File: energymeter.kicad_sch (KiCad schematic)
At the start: 43 parts, among them J1 CT1, J10 CT10, J11 LINE, J12 Conn_02x09_Odd_Even, J13 Conn_02x09_Odd_Even, J2 CT2, J3 CT3, J4 CT4, J5 CT5, J6 CT6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

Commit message: Updates
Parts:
- added J14: NEUTRAL, TerminalBlock_Phoenix:TerminalBlock_Phoenix_MKDS-1,5-2_1x02_P5.00mm_Horizontal, symbol Connector:Screw_Terminal_01x02
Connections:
- net at T1.2: now also J14.1 (Pin_1), J14.2 (Pin_2); no longer R67.1
- net at J11.1 (Pin_1), R65.2: now also J11.2 (Pin_2)
- net at R63.2: now also R67.1; no longer J11.2 (Pin_2)
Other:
- moved on the sheet: R65, R66, R67
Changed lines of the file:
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@@
 	)
 	(junction
-		(at 116.84 158.75)
+		(at 87.63 166.37)
 		(diameter 0)
 		(color 0 0 0 0)
@@
 	)
 	(junction
+		(at 87.63 153.67)
+		(diameter 0)
+		(color 0 0 0 0)
+	)
+	(junction
 		(at 162.56 144.78)
 		(diameter 0)
@@
 	(wire
 		(pts
-			(xy 97.79 158.75) (xy 99.06 158.75)
-		)
-		(stroke
-			(width 0)
-			(type default)
-		)
-	)
-	(wire
-		(pts
-			(xy 87.63 158.75) (xy 90.17 158.75)
+			(xy 97.79 153.67) (xy 99.06 153.67)
 		)
 		(stroke
@@
 	(wire
 		(pts
-			(xy 116.84 158.75) (xy 115.57 158.75)
+			(xy 116.84 166.37) (xy 87.63 166.37)
 		)
 		(stroke
@@
 	(wire
 		(pts
+			(xy 87.63 166.37) (xy 87.63 167.64)
+		)
+		(stroke
+			(width 0)
+			(type default)
+		)
+	)
+	(wire
+		(pts
+			(xy 115.57 153.67) (xy 116.84 153.67)
+		)
+		(stroke
+			(width 0)
+			(type default)
+		)
+	)
+	(wire
+		(pts
 			(xy 127 144.78) (xy 140.97 144.78)
 		)
@@
 	(wire
 		(pts
+			(xy 87.63 165.1) (xy 87.63 166.37)
+		)
+		(stroke
+			(width 0)
+			(type default)
+		)
+	)
+	(wire
+		(pts
 			(xy 105.41 38.1) (xy 105.41 41.91)
 		)
@@
 	(wire
 		(pts
+			(xy 87.63 152.4) (xy 87.63 153.67)
+		)
+		(stroke
+			(width 0)
+			(type default)
+		)
+	)
+	(wire
+		(pts
 			(xy 102.87 88.9) (xy 110.49 88.9)
 		)
@@
 	(wire
 		(pts
+			(xy 95.25 151.13) (xy 116.84 151.13)
+		)
+		(stroke
+			(width 0)
+			(type default)
+		)
+	)
+	(wire
+		(pts
 			(xy 217.17 144.78) (xy 217.17 146.05)
 		)
@@
 	(wire
 		(pts
-			(xy 106.68 158.75) (xy 107.95 158.75)
+			(xy 106.68 153.67) (xy 107.95 153.67)
 		)
 		(stroke
@@
 	(wire
 		(pts
+			(xy 116.84 151.13) (xy 116.84 153.67)
+		)
+		(stroke
+			(width 0)
+			(type default)
+		)
+	)
+	(wire
+		(pts
 			(xy 59.69 118.11) (xy 63.5 118.11)
 		)
@@
 	(wire
 		(pts
+			(xy 116.84 158.75) (xy 116.84 166.37)
+		)
+		(stroke
+			(width 0)
+			(type default)
+		)
+	)
+	(wire
+		(pts
 			(xy 27.94 29.21) (xy 27.94 27.94)
 		)
@@
 	(wire
 		(pts
-			(xy 119.38 158.75) (xy 116.84 158.75)
+			(xy 162.56 144.78) (xy 152.4 144.78)
 		)
 		(stroke
@@
 	(wire
 		(pts
-			(xy 162.56 144.78) (xy 152.4 144.78)
+			(xy 90.17 153.67) (xy 87.63 153.67)
 		)
 		(stroke
@@
 	(wire
 		(pts
+			(xy 87.63 153.67) (xy 87.63 154.94)
+		)
+		(stroke
+			(width 0)
+			(type default)
+		)
+	)
+	(wire
+		(pts
 			(xy 140.97 144.78) (xy 140.97 149.86)
 		)
@@
 	(wire
 		(pts
-			(xy 87.63 158.75) (xy 87.63 154.94)
-		)
-		(stroke
-			(width 0)
-			(type default)
-		)
-	)
-	(wire
-		(pts
 			(xy 218.44 95.25) (xy 218.44 97.79)
 		)
@@
 	(wire
 		(pts
-			(xy 87.63 148.59) (xy 87.63 152.4)
-		)
-		(stroke
-			(width 0)
-			(type default)
-		)
-	)
-	(wire
-		(pts
 			(xy 143.51 104.14) (xy 143.51 110.49)
 		)
@@
 	(wire
 		(pts
-			(xy 95.25 148.59) (xy 87.63 148.59)
-		)
-		(stroke
-			(width 0)
-			(type default)
-		)
-	)
-	(wire
-		(pts
 			(xy 218.44 57.15) (xy 220.98 57.15)
 		)
@@
 	(wire
 		(pts
+			(xy 95.25 148.59) (xy 95.25 151.13)
+		)
+		(stroke
+			(width 0)
+			(type default)
+		)
+	)
+	(wire
+		(pts
 			(xy 218.44 41.91) (xy 220.98 41.91)
 		)
@@
 	)
 	(symbol
+		(lib_id "Connector:Screw_Terminal_01x02")
+		(at 82.55 167.64 180)
+		(unit 1)
+		(exclude_from_sim no)
+		(in_bom yes)
+		(on_board yes)
+		(dnp no)
+		(fields_autoplaced yes)
+		(property "Reference" "J14"
+			(at 82.55 158.75 0)
+			(effects
+				(font
+					(size 1.27 1.27)
+				)
+			)
+		)
+		(property "Value" "NEUTRAL"
+			(at 82.55 161.29 0)
+			(effects
+				(font
+					(size 1.27 1.27)
+				)
+			)
+		)
+		(property "Footprint" "TerminalBlock_Phoenix:TerminalBlock_Phoenix_MKDS-1,5-2_1x02_P5.00mm_Horizontal"
+			(at 82.55 167.64 0)
+			(effects
+				(font
+					(size 1.27 1.27)
+				)
+				(hide yes)
+			)
+		)
+		(property "Datasheet" "~"
+			(at 82.55 167.64 0)
+			(effects
+				(font
+					(size 1.27 1.27)
+				)
+				(hide yes)
+			)
+		)
+		(property "Description" "Generic screw terminal, single row, 01x02, script generated (kicad-library-utils/schlib/autogen/connector/)"
+			(at 82.55 167.64 0)
+			(effects
+				(font
+					(size 1.27 1.27)
+				)
+				(hide yes)
+			)
+		)
+		(pin "2"
+		)
+		(pin "1"
+		)
+		(instances
+			(project "energymeter"
+				(path "/d5c3d4dc-7952-499c-ae9a-397827d02ad2"
+					(reference "J14")
+					(unit 1)
+				)
+			)
+		)
+	)
+	(symbol
 		(lib_id "power:+3.3V")
 		(at 259.08 128.27 0)
@@
 	(symbol
 		(lib_id "Device:R")
-		(at 111.76 158.75 270)
+		(at 111.76 153.67 270)
 		(unit 1)
 		(exclude_from_sim no)
@@
 		(fields_autoplaced yes)
 		(property "Reference" "R67"
-			(at 111.76 165.1 90)
+			(at 111.76 160.02 90)
 			(effects
 				(font
@@
 		)
 		(property "Value" "22K/1%"
-			(at 111.76 162.56 90)
+			(at 111.76 157.48 90)
 			(effects
 				(font
@@
 		)
 		(property "Footprint" "Resistor_SMD:R_0603_1608Metric"
-			(at 111.76 156.972 90)
+			(at 111.76 151.892 90)
 			(effects
 				(font
@@
 		)
 		(property "Datasheet" "~"
-			(at 111.76 158.75 0)
+			(at 111.76 153.67 0)
 			(effects
 				(font
@@
 		)
 		(property "Description" "Resistor"
-			(at 111.76 158.75 0)
+			(at 111.76 153.67 0)
 			(effects
 				(font
@@
 	(symbol
 		(lib_id "Device:R")
-		(at 102.87 158.75 270)
+		(at 102.87 153.67 270)
 		(unit 1)
 		(exclude_from_sim no)
@@
 		(fields_autoplaced yes)
 		(property "Reference" "R66"
-			(at 102.87 165.1 90)
+			(at 102.87 160.02 90)
 			(effects
 				(font
@@
 		)
 		(property "Value" "22K/1%"
-			(at 102.87 162.56 90)
+			(at 102.87 157.48 90)
 			(effects
 				(font
@@
 		)
 		(property "Footprint" "Resistor_SMD:R_0603_1608Metric"
-			(at 102.87 156.972 90)
+			(at 102.87 151.892 90)
 			(effects
 				(font
@@
 		)
 		(property "Datasheet" "~"
-			(at 102.87 158.75 0)
+			(at 102.87 153.67 0)
 			(effects
 				(font
@@
 		)
 		(property "Description" "Resistor"
-			(at 102.87 158.75 0)
+			(at 102.87 153.67 0)
 			(effects
 				(font
@@
 	(symbol
 		(lib_id "Device:R")
-		(at 93.98 158.75 270)
+		(at 93.98 153.67 270)
 		(unit 1)
 		(exclude_from_sim no)
@@
 		(fields_autoplaced yes)
 		(property "Reference" "R65"
-			(at 93.98 165.1 90)
+			(at 93.98 160.02 90)
 			(effects
 				(font
@@
 		)
 		(property "Value" "22K/1%"
-			(at 93.98 162.56 90)
+			(at 93.98 157.48 90)
 			(effects
 				(font
@@
 		)
 		(property "Footprint" "Resistor_SMD:R_0603_1608Metric"
-			(at 93.98 156.972 90)
+			(at 93.98 151.892 90)
 			(effects
 				(font
@@
 		)
 		(property "Datasheet" "~"
-			(at 93.98 158.75 0)
+			(at 93.98 153.67 0)
 			(effects
 				(font
@@
 		)
 		(property "Description" "Resistor"
-			(at 93.98 158.75 0)
+			(at 93.98 153.67 0)
 			(effects
 				(font

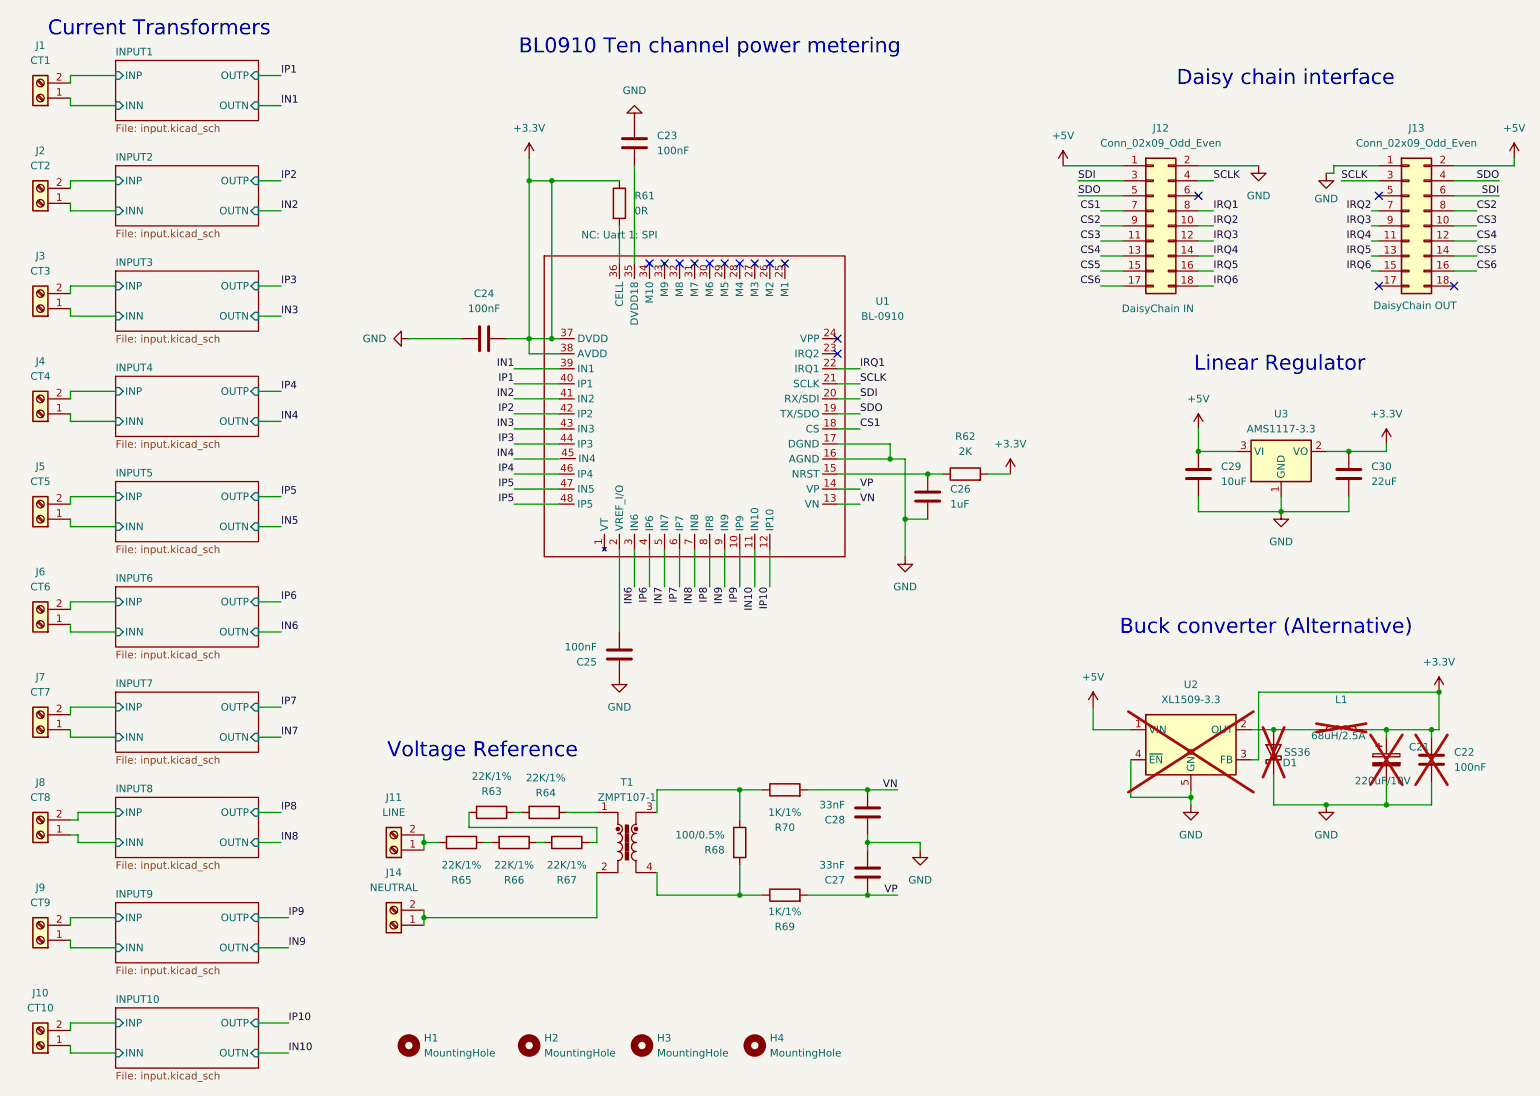
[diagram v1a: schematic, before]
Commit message: Change connector, assign JLCPCB
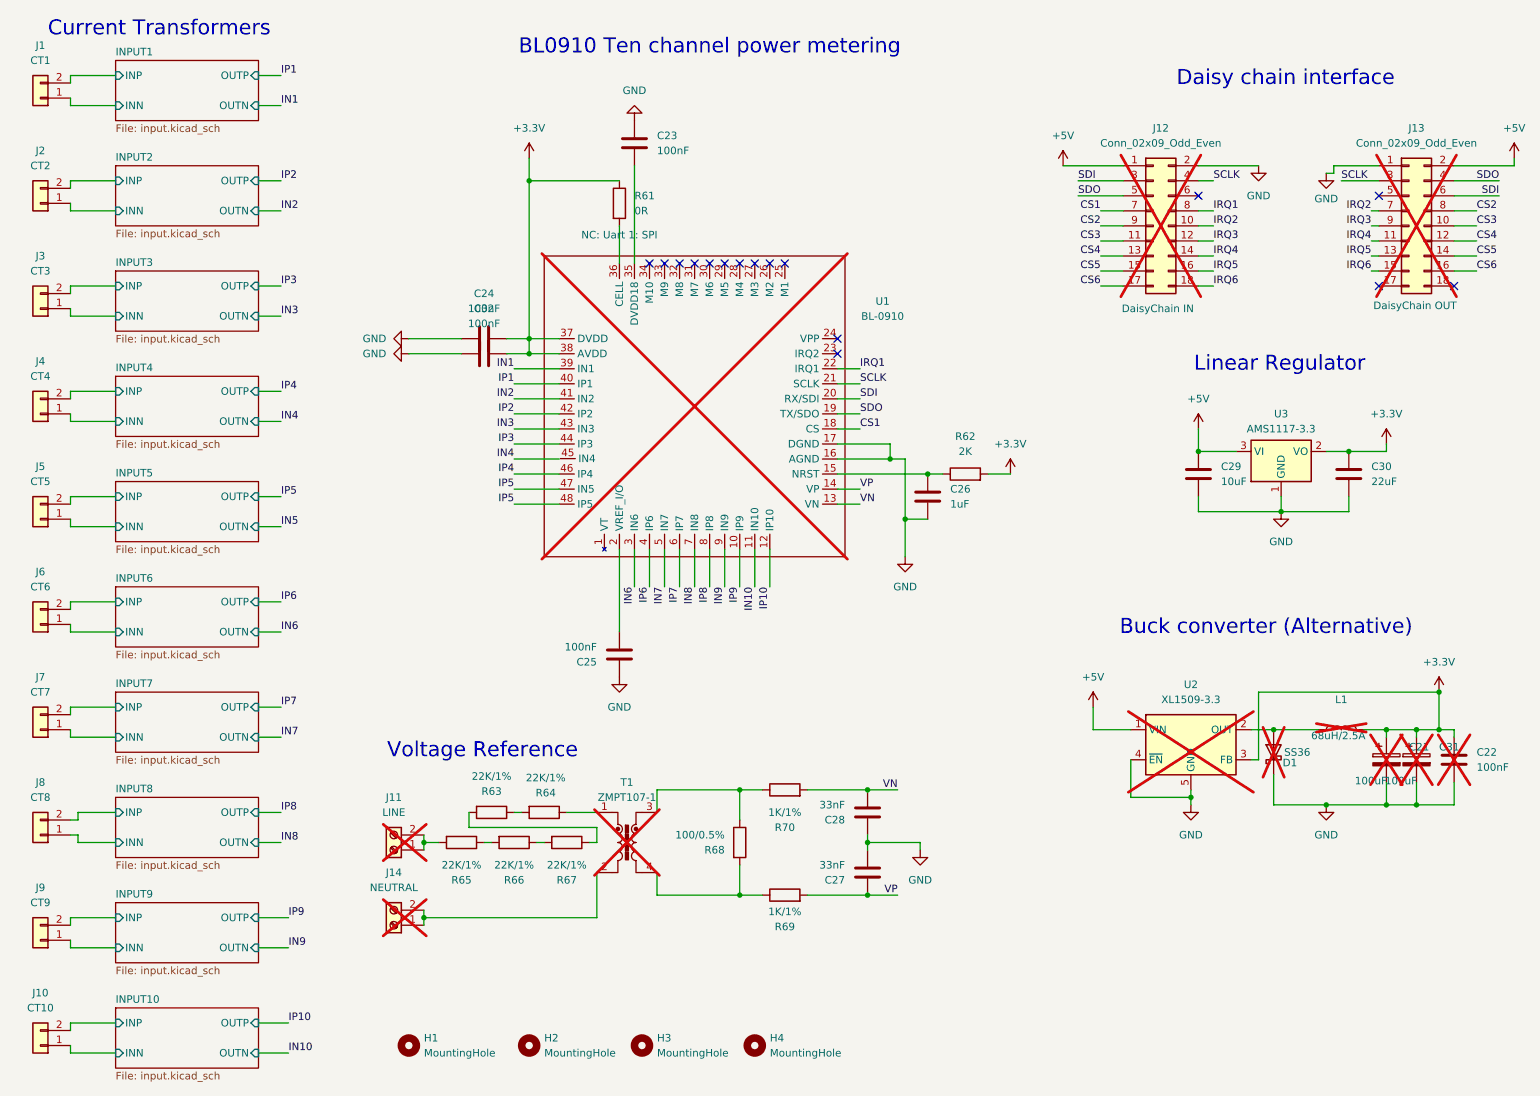
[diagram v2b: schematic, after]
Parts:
- added C31: 100uF, Capacitor_Tantalum_SMD:CP_EIA-3528-21_Kemet-B, symbol Device:C_Polarized
- added C32: 100nF, Capacitor_SMD:C_0603_1608Metric, symbol Device:C
- C21: value 220uF/10V -> 100uF; footprint (none) -> Capacitor_Tantalum_SMD:CP_EIA-3528-21_Kemet-B; LCSC (none) -> C16133
- C22, C23, C24, C25, C29: LCSC (none) -> C14858
- C26: LCSC (none) -> C15849
- C27, C28: LCSC (none) -> C21117
- C30: LCSC (none) -> C59461
- J1, J10, J2, J3, J4, J5, J6, J7, J8, J9: footprint TerminalBlock_Phoenix:TerminalBlock_Phoenix_MKDS-1,5-2_1x02_P5.00mm_Horizontal -> Connector_JST:JST_XH_B2B-XH-A_1x02_P2.50mm_Vertical; symbol Connector:Screw_Terminal_01x02 -> Connector_Generic:Conn_01x02; LCSC (none) -> C265283
- J11, J12, J13, J14, U1: now not fitted
- R61: LCSC (none) -> C21189
- R62: LCSC (none) -> C22975
- R63, R64, R65, R66, R67: LCSC (none) -> C31850
- R68: LCSC (none) -> C22775
- R69, R70: LCSC (none) -> C21190
- T1: LCSC (none) -> C125191; now not fitted
- U2: JLCPCB C61063 -> (none); LCSC (none) -> C61063
- U3: LCSC (none) -> C6186
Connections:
- net +3.3V: now also C31.1, C32.2
- net GND: now also C31.2, C32.1
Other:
- moved on the sheet: C22

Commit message: After layout
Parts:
- removed C22: 100nF, Capacitor_SMD:C_0603_1608Metric, symbol Device:C
- removed D1: SS36, Diode_SMD:D_SMA, symbol Diode:SS36
- removed L1: 68uH/2.5A, symbol Device:L
- removed U2: XL1509-3.3, Package_SO:SOIC-8_3.9x4.9mm_P1.27mm, symbol Regulator_Switching:XL1509-3.3
- C21, C31, J11, J12, J13, J14, T1, U1: now fitted
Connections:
- net IN4: now also U1.45 (IN4)
- net IN5: now also U1.47 (IN5)
- net IP5: no longer U1.47 (IN5)
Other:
- note added: "Capacitors"
- note removed: "Buck converter (Alternative)"

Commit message: First order
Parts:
- C21, C31: now in the parts list
- J11, J14: LCSC (none) -> C128027
- J12: value Conn_02x09_Odd_Even -> Conn_02x10_Odd_Even; footprint Connector_PinHeader_2.54mm:PinHeader_2x09_P2.54mm_Vertical -> Connector_PinHeader_2.54mm:PinHeader_2x10_P2.54mm_Vertical; symbol Connector_Generic:Conn_02x09_Odd_Even -> Connector_Generic:Conn_02x10_Odd_Even; LCSC (none) -> C5454488
- J13: value Conn_02x09_Odd_Even -> Conn_02x10_Odd_Even; footprint Connector_PinHeader_2.54mm:PinHeader_2x09_P2.54mm_Vertical -> Connector_PinHeader_2.54mm:PinHeader_2x10_P2.54mm_Vertical; symbol Connector_Generic:Conn_02x09_Odd_Even -> Connector_Generic:Conn_02x10_Odd_Even; LCSC (none) -> C239361
- U1: LCSC (none) -> C2841006
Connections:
- no-connect marks 16 -> 20
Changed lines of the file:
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@@
 	)
 	(no_connect
+		(at 218.44 62.23)
+	)
+	(no_connect
+		(at 248.92 62.23)
+	)
+	(no_connect
+		(at 261.62 62.23)
+	)
+	(no_connect
 		(at 146.05 55.88)
 	)
 	(no_connect
+		(at 205.74 62.23)
+	)
+	(no_connect
 		(at 128.27 55.88)
 	)
@@
 			)
 		)
-		(property "LCSC" ""
+		(property "LCSC" "C128027"
 			(at 82.55 167.64 0)
 			(effects
@@
 		(at 226.06 137.16 0)
 		(unit 1)
-		(exclude_from_sim yes)
-		(in_bom no)
+		(exclude_from_sim no)
+		(in_bom yes)
 		(on_board yes)
 		(dnp no)
@@
 			)
 		)
-		(property "LCSC" ""
+		(property "LCSC" "C128027"
 			(at 82.55 154.94 0)
 			(effects
@@
 		(at 233.68 137.16 0)
 		(unit 1)
-		(exclude_from_sim yes)
-		(in_bom no)
+		(exclude_from_sim no)
+		(in_bom yes)
 		(on_board yes)
 		(dnp no)
@@
 	)
 	(symbol
-		(lib_id "Connector_Generic:Conn_02x09_Odd_Even")
+		(lib_id "Connector_Generic:Conn_02x10_Odd_Even")
 		(at 254 49.53 0)
 		(unit 1)
@@
 			)
 		)
-		(property "Value" "Conn_02x09_Odd_Even"
+		(property "Value" "Conn_02x10_Odd_Even"
 			(at 255.27 35.56 0)
 			(effects
@@
 			)
 		)
-		(property "Footprint" "Connector_PinHeader_2.54mm:PinHeader_2x09_P2.54mm_Vertical"
+		(property "Footprint" "Connector_PinHeader_2.54mm:PinHeader_2x10_P2.54mm_Vertical"
 			(at 254 49.53 0)
 			(effects
@@
 		)
 		(property "Description" "DaisyChain OUT"
-			(at 255.016 62.992 0)
+			(at 255.27 65.786 0)
 			(effects
 				(font
@@
 			)
 		)
-		(property "LCSC" ""
+		(property "LCSC" "C239361"
 			(at 254 49.53 0)
 			(effects
@@
 		(pin "5"
 		)
+		(pin "19"
+		)
+		(pin "20"
+		)
 		(instances
 			(project "energymeter"
@@
 			)
 		)
-		(property "LCSC" ""
+		(property "LCSC" "C2841006"
 			(at 133.35 80.01 0)
 			(effects
@@
 	)
 	(symbol
-		(lib_id "Connector_Generic:Conn_02x09_Odd_Even")
+		(lib_id "Connector_Generic:Conn_02x10_Odd_Even")
 		(at 210.82 49.53 0)
 		(unit 1)
@@
 			)
 		)
-		(property "Value" "Conn_02x09_Odd_Even"
+		(property "Value" "Conn_02x10_Odd_Even"
 			(at 212.09 35.56 0)
 			(effects
@@
 			)
 		)
-		(property "Footprint" "Connector_PinHeader_2.54mm:PinHeader_2x09_P2.54mm_Vertical"
+		(property "Footprint" "Connector_PinHeader_2.54mm:PinHeader_2x10_P2.54mm_Vertical"
 			(at 210.82 49.53 0)
 			(effects
@@
 		)
 		(property "Description" "DaisyChain IN"
-			(at 211.582 63.5 0)
+			(at 211.836 65.786 0)
 			(effects
 				(font
@@
 			)
 		)
-		(property "LCSC" ""
+		(property "LCSC" "C5454488"
 			(at 210.82 49.53 0)
 			(effects
@@
 		(pin "5"
 		)
+		(pin "19"
+		)
+		(pin "20"
+		)
 		(instances

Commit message: WIP
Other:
- note added: "U2 = (U1 / R') * R U2 = (230 / (22K * 5)) * 100 U2 = 0.209V RMS, 0.295V Vpeak Limit is +-0.7V Vpeak"
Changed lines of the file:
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@@
+		)
+	)
+	(text "U2 = (U1 / R') * R\nU2 = (230 / (22K * 5)) * 100\nU2 = 0.209V RMS, 0.295V Vpeak\nLimit is +-0.7V Vpeak\n"
+		(exclude_from_sim no)
+		(at 128.778 169.418 0)
+		(effects
+			(font
+				(size 1.27 1.27)
+			)
 		)
 	)
